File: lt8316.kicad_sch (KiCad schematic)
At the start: 20 parts, among them Q1 TK3P80E,RQ, U1 LT8316EFE

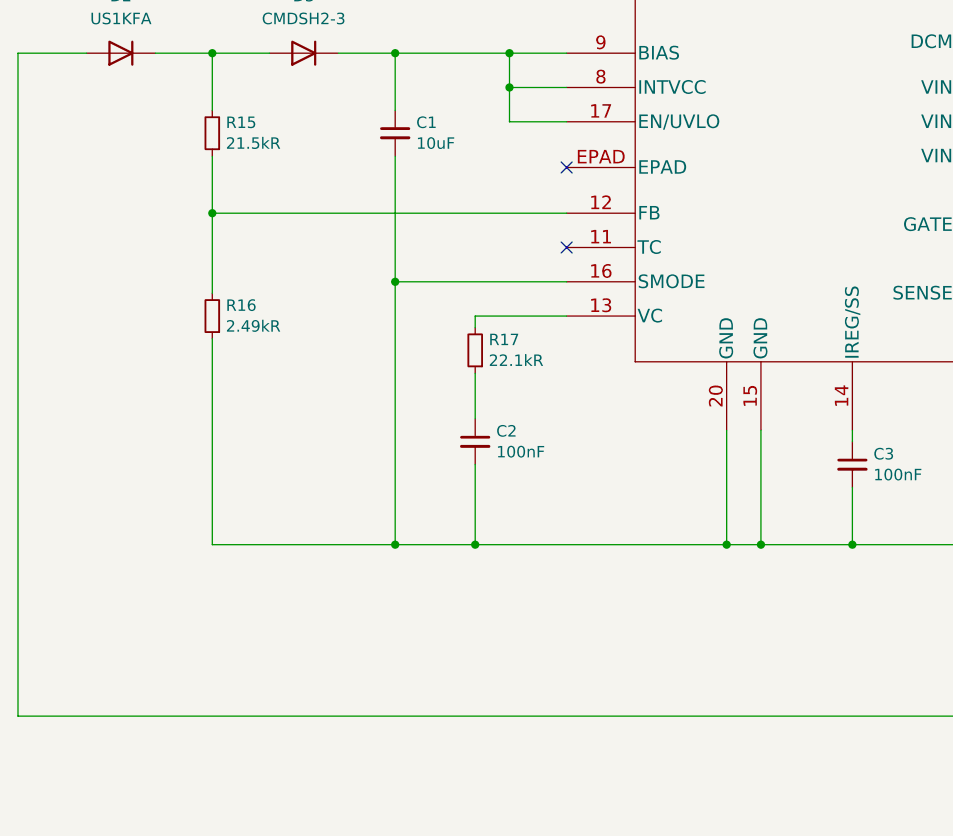
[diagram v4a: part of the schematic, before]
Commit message: resistors change; elements placed; new footprints
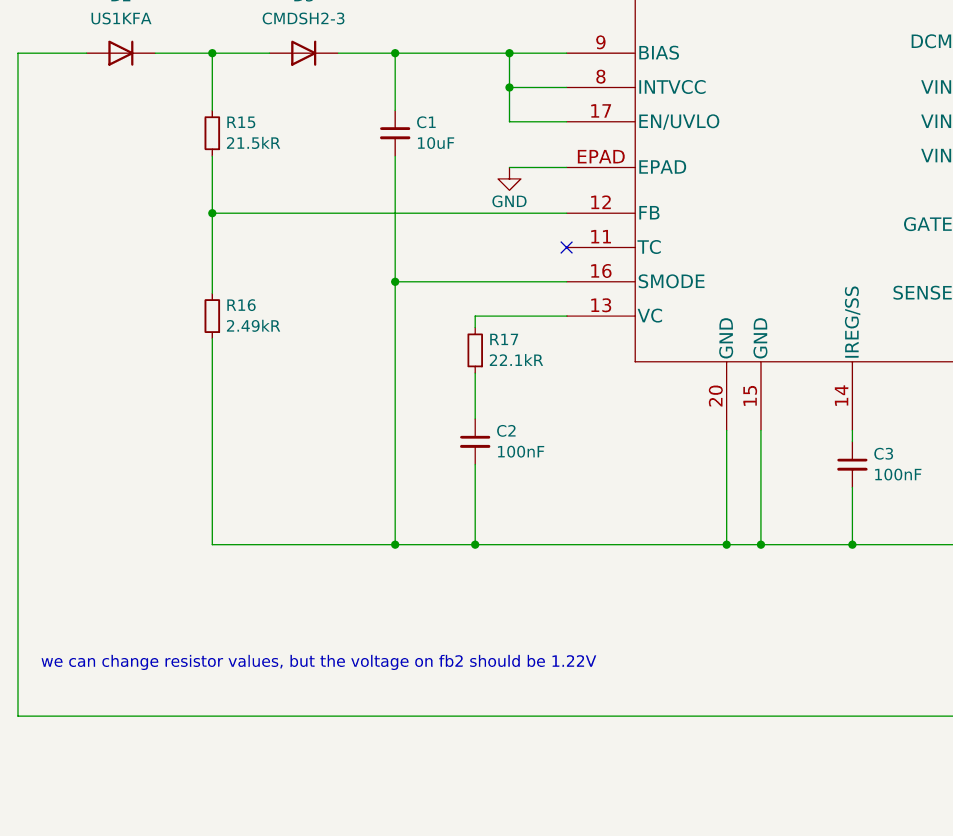
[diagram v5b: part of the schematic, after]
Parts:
- C1, C2, C3, C6, C7, C8: footprint Capacitor_SMD:C_1206_3216Metric -> Capacitor_SMD:C_0603_1608Metric
- R15, R16, R17, R19: footprint Resistor_SMD:R_1206_3216Metric -> Resistor_SMD:R_0603_1608Metric
- U1: footprint Package_SO:TSSOP-20_4.4x6.5mm_P0.65mm -> vindicator:LT8316EFE
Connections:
- net GND: now also U1.EPAD
- no-connect marks 2 -> 1
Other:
- note added: "we can change resistor values, but the voltage on fb2 should be 1.22V"

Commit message: pcb edit
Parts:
- C2, C3: footprint Capacitor_SMD:C_0603_1608Metric -> Capacitor_SMD:C_1812_4532Metric
- C4: footprint Capacitor_SMD:C_1206_3216Metric -> Capacitor_SMD:C_1812_4532Metric
- C6, C7, C8: footprint Capacitor_SMD:C_0603_1608Metric -> Capacitor_SMD:C_1206_3216Metric
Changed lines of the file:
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@@
       (effects (font (size 1.27 1.27)) (justify left))
     )
-    (property "Footprint" "Capacitor_SMD:C_1206_3216Metric" (id 2) (at 176.53 34.29 0)
+    (property "Footprint" "Capacitor_SMD:C_1812_4532Metric" (id 2) (at 176.53 34.29 0)
       (effects (font (size 1.27 1.27)) hide)
     )
@@
       (effects (font (size 1.27 1.27)) (justify left))
     )
-    (property "Footprint" "Capacitor_SMD:C_0603_1608Metric" (id 2) (at 250.19 135.89 0)
+    (property "Footprint" "Capacitor_SMD:C_1206_3216Metric" (id 2) (at 250.19 135.89 0)
       (effects (font (size 1.27 1.27)) hide)
     )
@@
       (effects (font (size 1.27 1.27)) (justify left))
     )
-    (property "Footprint" "Capacitor_SMD:C_0603_1608Metric" (id 2) (at 148.59 107.95 0)
+    (property "Footprint" "Capacitor_SMD:C_1812_4532Metric" (id 2) (at 148.59 107.95 0)
       (effects (font (size 1.27 1.27)) hide)
     )
@@
       (effects (font (size 1.27 1.27)) (justify left))
     )
-    (property "Footprint" "Capacitor_SMD:C_0603_1608Metric" (id 2) (at 240.03 135.89 0)
+    (property "Footprint" "Capacitor_SMD:C_1206_3216Metric" (id 2) (at 240.03 135.89 0)
       (effects (font (size 1.27 1.27)) hide)
     )
@@
       (effects (font (size 1.27 1.27)) (justify left))
     )
-    (property "Footprint" "Capacitor_SMD:C_0603_1608Metric" (id 2) (at 261.62 135.89 0)
+    (property "Footprint" "Capacitor_SMD:C_1206_3216Metric" (id 2) (at 261.62 135.89 0)
       (effects (font (size 1.27 1.27)) hide)
     )
@@
       (effects (font (size 1.27 1.27)) (justify left))
     )
-    (property "Footprint" "Capacitor_SMD:C_0603_1608Metric" (id 2) (at 106.68 105.41 0)
-      (effects (font (size 1.27 1.27)) hide)
-    )
+    (property "Footprint" "Capacitor_SMD:C_1812_4532Metric" (id 2) (at 106.68 105.41 0)
+      (effects (font (size 1.27 1.27)) hide)
+    )

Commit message: pcb update
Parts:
- C2, C3: footprint Capacitor_SMD:C_1812_4532Metric -> Capacitor_SMD:C_0603_1608Metric
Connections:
- net GND: no longer U1.EPAD
- net at C1.2, C2.2, C3.2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: now also U1.EPAD
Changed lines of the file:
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@@
   (junction (at 205.74 88.9) (diameter 0) (color 0 0 0 0)
+  )
+  (junction (at 88.9 116.84) (diameter 0) (color 0 0 0 0)
   )
   (junction (at 110.49 66.04) (diameter 0) (color 0 0 0 0)
@@
     (stroke (width 0) (type default) (color 0 0 0 0))
   )
+  (wire (pts (xy 88.9 116.84) (xy 97.79 116.84))
+    (stroke (width 0) (type default) (color 0 0 0 0))
+  )
   (wire (pts (xy 77.47 80.01) (xy 77.47 88.9))
     (stroke (width 0) (type default) (color 0 0 0 0))
@@
     (stroke (width 0) (type default) (color 0 0 0 0))
   )
-  (wire (pts (xy 110.49 74.93) (xy 116.84 74.93))
+  (wire (pts (xy 88.9 74.93) (xy 116.84 74.93))
     (stroke (width 0) (type default) (color 0 0 0 0))
   )
@@
     (stroke (width 0) (type default) (color 0 0 0 0))
   )
-  (wire (pts (xy 77.47 116.84) (xy 97.79 116.84))
+  (wire (pts (xy 88.9 74.93) (xy 88.9 116.84))
+    (stroke (width 0) (type default) (color 0 0 0 0))
+  )
+  (wire (pts (xy 77.47 116.84) (xy 88.9 116.84))
     (stroke (width 0) (type default) (color 0 0 0 0))
   )
@@
       (effects (font (size 1.27 1.27)) (justify left))
     )
-    (property "Footprint" "Capacitor_SMD:C_1812_4532Metric" (id 2) (at 148.59 107.95 0)
+    (property "Footprint" "Capacitor_SMD:C_0603_1608Metric" (id 2) (at 148.59 107.95 0)
       (effects (font (size 1.27 1.27)) hide)
     )
@@
     (pin "1")
     (pin "2")
-  )
-  (symbol (lib_id "power:GND") (at 110.49 74.93 0) (unit 1)
-    (in_bom yes) (on_board yes)
-    (property "Reference" "#PWR0113" (id 0) (at 110.49 81.28 0)
-      (effects (font (size 1.27 1.27)) hide)
-    )
-    (property "Value" "GND" (id 1) (at 110.49 78.74 0))
-    (property "Footprint" "" (id 2) (at 110.49 74.93 0)
-      (effects (font (size 1.27 1.27)) hide)
-    )
-    (property "Datasheet" "" (id 3) (at 110.49 74.93 0)
-      (effects (font (size 1.27 1.27)) hide)
-    )
-    (pin "1")
   )
   (symbol (lib_id "Diode:US1K") (at 67.31 62.23 180) (unit 1)
@@
       (effects (font (size 1.27 1.27)) (justify left))
     )
-    (property "Footprint" "Capacitor_SMD:C_1812_4532Metric" (id 2) (at 106.68 105.41 0)
-      (effects (font (size 1.27 1.27)) hide)
-    )
+    (property "Footprint" "Capacitor_SMD:C_0603_1608Metric" (id 2) (at 106.68 105.41 0)
+      (effects (font (size 1.27 1.27)) hide)
+    )

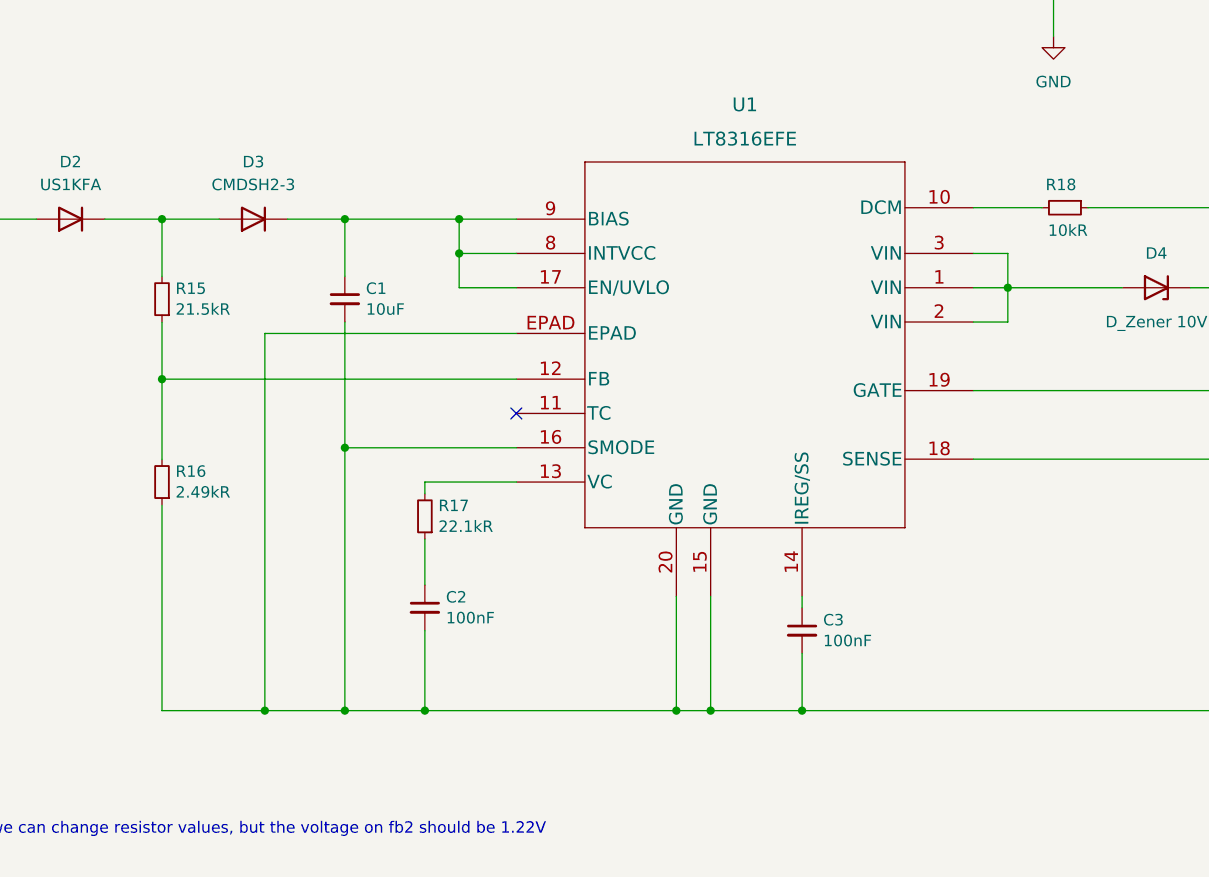
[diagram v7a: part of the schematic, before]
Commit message: symbol changed / resistor values changed
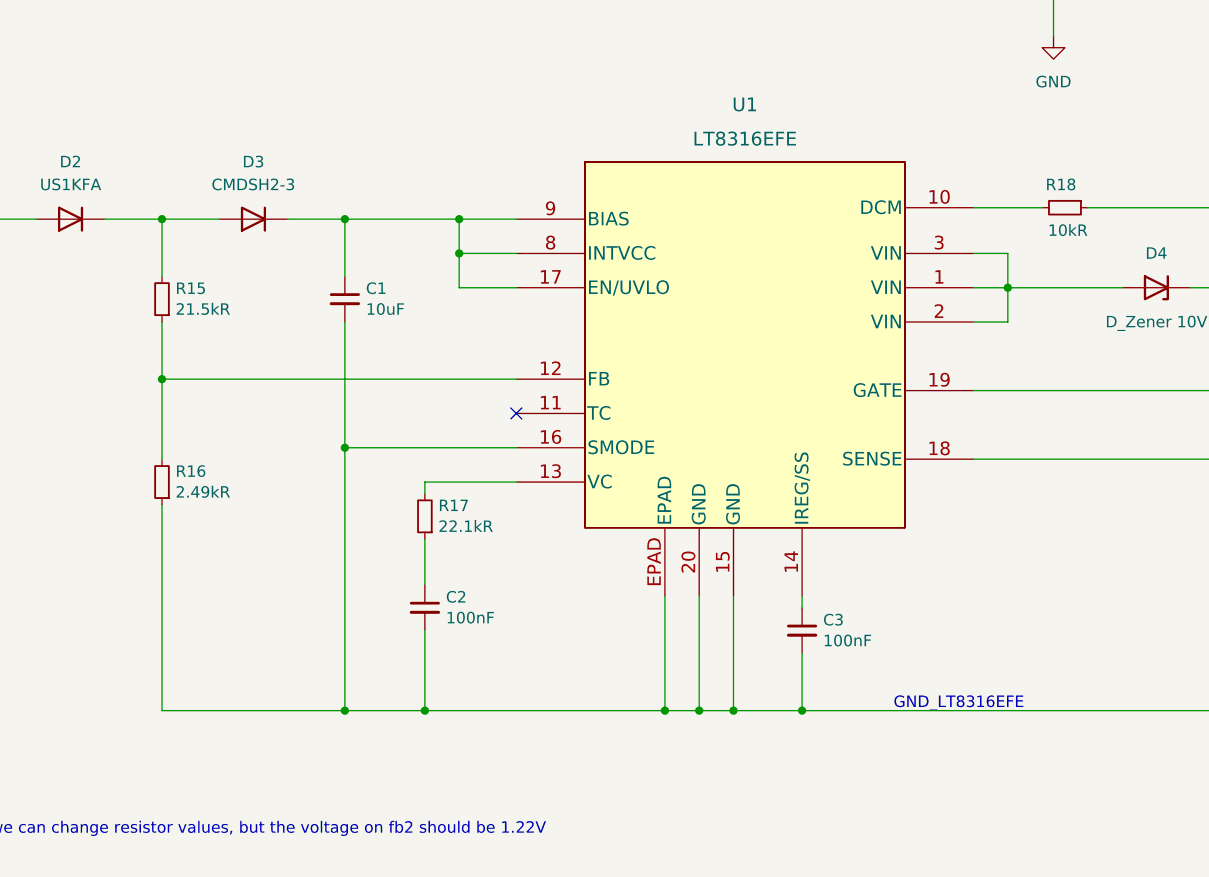
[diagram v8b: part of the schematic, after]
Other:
- note added: "GND_LT8316EFE"
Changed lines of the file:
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@@
   (junction (at 205.74 88.9) (diameter 0) (color 0 0 0 0)
   )
-  (junction (at 88.9 116.84) (diameter 0) (color 0 0 0 0)
+  (junction (at 133.35 116.84) (diameter 0) (color 0 0 0 0)
   )
   (junction (at 110.49 66.04) (diameter 0) (color 0 0 0 0)
@@
   (junction (at 250.19 139.7) (diameter 0) (color 0 0 0 0)
   )
-  (junction (at 138.43 116.84) (diameter 0) (color 0 0 0 0)
-  )
-  (junction (at 134.62 116.84) (diameter 0) (color 0 0 0 0)
+  (junction (at 137.16 116.84) (diameter 0) (color 0 0 0 0)
   )
   (junction (at 148.59 116.84) (diameter 0) (color 0 0 0 0)
+  )
+  (junction (at 140.97 116.84) (diameter 0) (color 0 0 0 0)
   )
   (junction (at 250.19 132.08) (diameter 0) (color 0 0 0 0)
@@
     (stroke (width 0) (type default) (color 0 0 0 0))
   )
-  (wire (pts (xy 88.9 116.84) (xy 97.79 116.84))
+  (wire (pts (xy 133.35 104.14) (xy 133.35 116.84))
+    (stroke (width 0) (type default) (color 0 0 0 0))
+  )
+  (wire (pts (xy 77.47 116.84) (xy 97.79 116.84))
     (stroke (width 0) (type default) (color 0 0 0 0))
   )
@@
     (stroke (width 0) (type default) (color 0 0 0 0))
   )
-  (wire (pts (xy 138.43 116.84) (xy 134.62 116.84))
-    (stroke (width 0) (type default) (color 0 0 0 0))
-  )
   (wire (pts (xy 199.39 60.96) (xy 205.74 60.96))
     (stroke (width 0) (type default) (color 0 0 0 0))
@@
     (stroke (width 0) (type default) (color 0 0 0 0))
   )
+  (wire (pts (xy 133.35 116.84) (xy 137.16 116.84))
+    (stroke (width 0) (type default) (color 0 0 0 0))
+  )
   (wire (pts (xy 106.68 91.44) (xy 106.68 92.71))
     (stroke (width 0) (type default) (color 0 0 0 0))
@@
     (stroke (width 0) (type default) (color 0 0 0 0))
   )
+  (wire (pts (xy 137.16 116.84) (xy 140.97 116.84))
+    (stroke (width 0) (type default) (color 0 0 0 0))
+  )
   (wire (pts (xy 110.49 66.04) (xy 110.49 62.23))
     (stroke (width 0) (type default) (color 0 0 0 0))
@@
     (stroke (width 0) (type default) (color 0 0 0 0))
   )
-  (wire (pts (xy 138.43 104.14) (xy 138.43 116.84))
+  (wire (pts (xy 140.97 104.14) (xy 140.97 116.84))
     (stroke (width 0) (type default) (color 0 0 0 0))
   )
@@
     (stroke (width 0) (type default) (color 0 0 0 0))
   )
-  (wire (pts (xy 88.9 74.93) (xy 116.84 74.93))
-    (stroke (width 0) (type default) (color 0 0 0 0))
-  )
   (wire (pts (xy 97.79 87.63) (xy 97.79 116.84))
     (stroke (width 0) (type default) (color 0 0 0 0))
   )
-  (wire (pts (xy 148.59 116.84) (xy 138.43 116.84))
+  (wire (pts (xy 148.59 116.84) (xy 140.97 116.84))
     (stroke (width 0) (type default) (color 0 0 0 0))
   )
@@
     (stroke (width 0) (type default) (color 0 0 0 0))
   )
-  (wire (pts (xy 134.62 116.84) (xy 106.68 116.84))
+  (wire (pts (xy 106.68 116.84) (xy 133.35 116.84))
     (stroke (width 0) (type default) (color 0 0 0 0))
   )
@@
     (stroke (width 0) (type default) (color 0 0 0 0))
   )
-  (wire (pts (xy 134.62 104.14) (xy 134.62 116.84))
+  (wire (pts (xy 137.16 104.14) (xy 137.16 116.84))
     (stroke (width 0) (type default) (color 0 0 0 0))
   )
@@
   )
   (wire (pts (xy 176.53 36.83) (xy 176.53 41.91))
-    (stroke (width 0) (type default) (color 0 0 0 0))
-  )
-  (wire (pts (xy 88.9 74.93) (xy 88.9 116.84))
-    (stroke (width 0) (type default) (color 0 0 0 0))
-  )
-  (wire (pts (xy 77.47 116.84) (xy 88.9 116.84))
     (stroke (width 0) (type default) (color 0 0 0 0))
   )
@@
     (effects (font (size 1.27 1.27)) (justify left bottom))
   )
+  (text "GND_LT8316EFE" (at 158.75 116.84 0)
+    (effects (font (size 1.27 1.27)) (justify left bottom))
+  )
